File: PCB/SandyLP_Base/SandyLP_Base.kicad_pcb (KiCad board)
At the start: 2 copper layers, 275.5 x 80.3 mm, 228 parts, among them J1 Conn_01x10_Pin, J2 Conn_01x01_Pin, J3 Conn_02x02_Odd_Even, J7 USB_C_Receptacle_USB2.0, J8 Conn_01x03, Q1 BSS138, SW1 BOOT, SW3 BOOT_ALT, U1 NCP1117-3.3_SOT223, U2 RP2040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

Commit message: Mid-ISOの中央ネジがソケットのパッドに近すぎるので、少し上へ移動
USBのD+、D-なども合わせて調整。
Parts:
- moved H_mid_13 0.60 mm to (273.5, 45.5)
- moved H_mid_9 0.60 mm to (44.9, 45.5)
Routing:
- net D-: track 23.8 -> 24.4 mm
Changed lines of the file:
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@@
 		(fp_arc
 			(start -0.378178 -1.358526)
-			(mid -0.787709 -1.474533)
+			(mid -0.787708 -1.474533)
 			(end -0.8 -1.9)
 			(stroke
@@
 		(fp_arc
 			(start -0.378178 -1.358526)
-			(mid -0.787709 -1.474533)
+			(mid -0.787708 -1.474533)
 			(end -0.8 -1.9)
 			(stroke
@@
 	(footprint "locallib:MountingHole_1.8-2.2mm_M2_Pad_minimal"
 		(layer "B.Cu")
-		(at 44.870935 46.053405 180)
+		(at 44.870935 45.458102 180)
 		(descr "Mounting Hole 2.2mm, M2")
 		(tags "mounting hole 2.2mm m2")
@@
 	(footprint "locallib:MountingHole_1.8-2.2mm_M2_Pad_minimal"
 		(layer "B.Cu")
-		(at 273.470935 46.053405 180)
+		(at 273.470935 45.458102 180)
 		(descr "Mounting Hole 2.2mm, M2")
 		(tags "mounting hole 2.2mm m2")
@@
 	)
 	(segment
-		(start 51.428434 43.574655)
-		(end 42.524685 43.574655)
-		(width 0.5)
+		(start 35.045935 43.393813)
+		(end 35.045935 43.117115)
+		(width 0.381)
 		(layer "B.Cu")
 		(net 22)
 	)
 	(segment
-		(start 35.045935 43.393813)
-		(end 35.045935 43.117115)
-		(width 0.381)
+		(start 40.614685 45.484655)
+		(end 37.308435 45.484655)
+		(width 0.5)
 		(layer "B.Cu")
 		(net 22)
@@
 	)
 	(segment
-		(start 40.614685 45.484655)
-		(end 37.308435 45.484655)
-		(width 0.5)
+		(start 34.095935 42.092115)
+		(end 34.095935 43.121115)
+		(width 0.254)
 		(layer "B.Cu")
 		(net 22)
@@
 	)
 	(segment
-		(start 34.258435 43.184655)
-		(end 34.978395 43.184655)
-		(width 0.254)
+		(start 50.930629 43.07685)
+		(end 43.02249 43.07685)
+		(width 0.5)
+		(layer "B.Cu")
+		(net 22)
+	)
+	(segment
+		(start 43.02249 43.07685)
+		(end 40.614685 45.484655)
+		(width 0.5)
 		(layer "B.Cu")
 		(net 22)
@@
 	)
 	(segment
-		(start 34.095935 42.092115)
-		(end 34.095935 43.022155)
-		(width 0.254)
-		(layer "B.Cu")
-		(net 22)
-	)
-	(segment
-		(start 42.524685 43.574655)
-		(end 40.614685 45.484655)
+		(start 37.308435 45.484655)
+		(end 36.408435 46.384655)
 		(width 0.5)
 		(layer "B.Cu")
@@
 	)
 	(segment
-		(start 37.308435 45.484655)
-		(end 36.408435 46.384655)
-		(width 0.5)
+		(start 35.598935 43.946813)
+		(end 35.045935 43.393813)
+		(width 0.381)
 		(layer "B.Cu")
 		(net 22)
 	)
 	(segment
-		(start 34.095935 43.022155)
-		(end 34.258435 43.184655)
+		(start 35.095935 43.067115)
+		(end 35.045935 43.117115)
 		(width 0.254)
 		(layer "B.Cu")
@@
 	)
 	(segment
-		(start 35.598935 43.946813)
-		(end 35.045935 43.393813)
-		(width 0.381)
+		(start 35.095935 42.092115)
+		(end 35.095935 43.067115)
+		(width 0.254)
 		(layer "B.Cu")
 		(net 22)
 	)
 	(segment
-		(start 51.858435 44.004656)
-		(end 51.428434 43.574655)
-		(width 0.5)
+		(start 34.368633 43.393813)
+		(end 35.045935 43.393813)
+		(width 0.254)
 		(layer "B.Cu")
 		(net 22)
 	)
 	(segment
-		(start 35.095935 43.067115)
-		(end 35.045935 43.117115)
+		(start 34.095935 43.121115)
+		(end 34.368633 43.393813)
 		(width 0.254)
 		(layer "B.Cu")
@@
 	)
 	(segment
-		(start 35.095935 42.092115)
-		(end 35.095935 43.067115)
-		(width 0.254)
+		(start 51.858435 44.004656)
+		(end 50.930629 43.07685)
+		(width 0.5)
 		(layer "B.Cu")
 		(net 22)
@@
 	)
 	(segment
-		(start 49.370935 42.178405)
-		(end 49.870935 42.178405)
+		(start 44.858435 42.347155)
+		(end 45.258435 41.947155)
 		(width 0.5)
 		(layer "B.Cu")
@@
 	)
 	(segment
-		(start 36.808435 44.784655)
-		(end 40.324735 44.784655)
+		(start 40.324735 44.784655)
+		(end 43.162235 41.947155)
+		(width 0.5)
+		(layer "B.Cu")
+		(net 23)
+	)
+	(segment
+		(start 46.72874 42.37685)
+		(end 47.158435 41.947155)
+		(width 0.5)
+		(layer "B.Cu")
+		(net 23)
+	)
+	(segment
+		(start 43.162235 41.947155)
+		(end 43.858435 41.947155)
+		(width 0.5)
+		(layer "B.Cu")
+		(net 23)
+	)
+	(segment
+		(start 36.408435 44.384655)
+		(end 36.808435 44.784655)
+		(width 0.5)
+		(layer "B.Cu")
+		(net 23)
+	)
+	(segment
+		(start 43.858435 41.947155)
+		(end 44.258435 42.347155)
+		(width 0.5)
+		(layer "B.Cu")
+		(net 23)
+	)
+	(segment
+		(start 52.958435 42.647155)
+		(end 52.958435 44.004656)
+		(width 0.5)
+		(layer "B.Cu")
+		(net 23)
+	)
+	(segment
+		(start 45.82874 41.947155)
+		(end 46.258435 42.37685)
 		(width 0.5)
 		(layer "B.Cu")
@@
 	)
 	(segment
-		(start 51.670935 42.178405)
-		(end 52.620935 42.178405)
+		(start 48.658435 42.347155)
+		(end 49.058435 41.947155)
 		(width 0.5)
 		(layer "B.Cu")
@@
 	)
 	(segment
-		(start 34.595935 42.092115)
-		(end 34.595935 41.247155)
-		(width 0.254)
+		(start 48.158435 42.347155)
+		(end 48.658435 42.347155)
+		(width 0.5)
 		(layer "B.Cu")
 		(net 23)
 	)
 	(segment
-		(start 51.220935 42.628405)
-		(end 51.670935 42.178405)
-		(width 0.5)
+		(start 34.595935 42.092115)
+		(end 34.595935 41.247155)
+		(width 0.254)
 		(layer "B.Cu")
 		(net 23)
 	)
 	(segment
-		(start 53.290935 43.672156)
-		(end 52.958435 44.004656)
+		(start 47.158435 41.947155)
+		(end 47.758435 41.947155)
 		(width 0.5)
 		(layer "B.Cu")
@@
 	)
 	(segment
-		(start 50.320935 42.628405)
-		(end 51.220935 42.628405)
+		(start 50.358435 42.347155)
+		(end 52.658435 42.347155)
 		(width 0.5)
 		(layer "B.Cu")
@@
 	)
 	(segment
-		(start 53.290935 42.848405)
-		(end 53.290935 43.672156)
+		(start 46.258435 42.37685)
+		(end 46.72874 42.37685)
 		(width 0.5)
 		(layer "B.Cu")
@@
 	)
 	(segment
-		(start 42.234735 42.874655)
-		(end 48.674685 42.874655)
+		(start 52.658435 42.347155)
+		(end 52.958435 42.647155)
+		(width 0.5)
+		(layer "B.Cu")
+		(net 23)
+	)
+	(segment
+		(start 36.808435 44.784655)
+		(end 40.324735 44.784655)
 		(width 0.5)
 		(layer "B.Cu")
@@
 	)
 	(segment
-		(start 52.620935 42.178405)
-		(end 53.290935 42.848405)
+		(start 44.258435 42.347155)
+		(end 44.858435 42.347155)
 		(width 0.5)
 		(layer "B.Cu")
@@
 	)
 	(segment
-		(start 49.870935 42.178405)
-		(end 50.320935 42.628405)
+		(start 49.058435 41.947155)
+		(end 49.958435 41.947155)
 		(width 0.5)
 		(layer "B.Cu")
@@
 	)
 	(segment
-		(start 40.324735 44.784655)
-		(end 42.234735 42.874655)
+		(start 49.958435 41.947155)
+		(end 50.358435 42.347155)
 		(width 0.5)
 		(layer "B.Cu")
@@
 	)
 	(segment
-		(start 36.408435 44.384655)
-		(end 36.808435 44.784655)
+		(start 47.758435 41.947155)
+		(end 48.158435 42.347155)
 		(width 0.5)
 		(layer "B.Cu")
@@
 	)
 	(segment
-		(start 48.674685 42.874655)
-		(end 49.370935 42.178405)
+		(start 45.258435 41.947155)
+		(end 45.82874 41.947155)
 		(width 0.5)
 		(layer "B.Cu")
@@
 	)
 	(via
-		(at 41.970935 42.028405)
+		(at 41.89439 41.886224)
 		(size 0.8)
 		(drill 0.4)
@@
 	)
 	(via
+		(at 53.508435 41.697155)
+		(size 0.8)
+		(drill 0.4)
+		(layers "F.Cu" "B.Cu")
+		(free yes)
+		(net 91)
+	)
+	(via
 		(at 23.870935 44.928405)
 		(size 0.8)
@@
 	)
 	(via
-		(at 52.270935 43.118405)
-		(size 0.8)
-		(drill 0.4)
-		(layers "F.Cu" "B.Cu")
-		(free yes)
-		(net 91)
-	)
-	(via
 		(at 159.171051 113.919101)
 		(size 0.8)
@@
 	)
 	(via
-		(at 37.608435 43.934655)
+		(at 37.458435 43.934655)
 		(size 0.8)
 		(drill 0.4)
@@
 	)
 	(via
-		(at 50.770935 41.628405)
+		(at 48.408435 41.147155)
 		(size 0.8)
 		(drill 0.4)
@@
 	)
 	(via
-		(at 44.870935 41.978405)
+		(at 44.558435 41.147155)
 		(size 0.8)
 		(drill 0.4)
@@
 	)
 	(via
-		(at 48.270935 41.978405)
+		(at 46.508435 41.147155)
 		(size 0.8)
 		(drill 0.4)
@@
 	)
 	(via
-		(at 53.370935 41.628405)
+		(at 51.158435 41.147155)
 		(size 0.8)
 		(drill 0.4)
@@
 	)
 	(via
-		(at 54.270935 43.128405)
+		(at 54.058435 43.128405)
 		(size 0.8)
 		(drill 0.4)

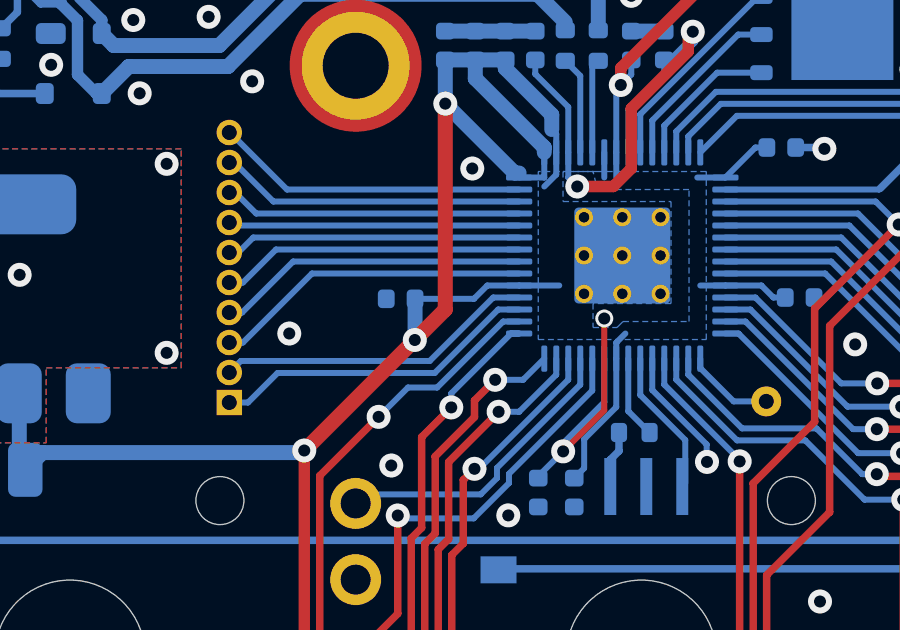
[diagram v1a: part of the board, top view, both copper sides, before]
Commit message: MCUまわりのCを近づける
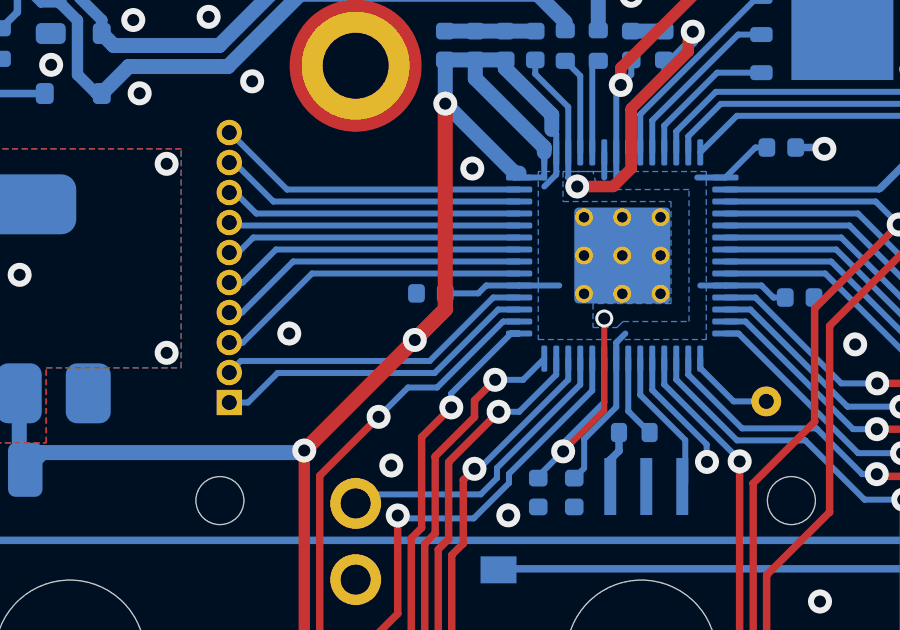
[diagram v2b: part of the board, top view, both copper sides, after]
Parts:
- moved C8 1.02 mm to (47.4, 53.0)
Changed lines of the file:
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@@
 		(fp_arc
 			(start -0.378178 -1.358526)
-			(mid -0.787708 -1.474533)
+			(mid -0.787709 -1.474533)
 			(end -0.8 -1.9)
 			(stroke
@@
 		(fp_arc
 			(start -0.378178 -1.358526)
-			(mid -0.787708 -1.474533)
+			(mid -0.787709 -1.474533)
 			(end -0.8 -1.9)
 			(stroke
@@
 	(footprint "Capacitor_SMD:C_0402_1005Metric"
 		(layer "B.Cu")
-		(at 46.370935 53.228405 180)
+		(at 47.378435 53.047155 180)
 		(descr "Capacitor SMD 0402 (1005 Metric), square (rectangular) end terminal, IPC_7351 nominal, (Body size source: IPC-SM-782 page 76, https://www.pcb-3d.com/wordpress/wp-content/uploads/ipc-sm-782a_amendment_1_and_2.pdf), generated with kicad-footprint-generator")
 		(tags "capacitor")
@@
 	)
 	(segment
-		(start 48.814685 53.228405)
-		(end 46.850935 53.228405)
-		(width 0.2)
-		(layer "B.Cu")
-		(net 1)
-	)
-	(segment
 		(start 57.195935 49.184655)
 		(end 58.195935 48.184655)
@@
 	)
 	(segment
+		(start 46.842809 54.600281)
+		(end 47.858435 53.584655)
+		(width 0.5)
+		(layer "B.Cu")
+		(net 1)
+	)
+	(segment
 		(start 55.878435 41.364655)
 		(end 55.858435 41.344655)
@@
 	)
 	(segment
-		(start 46.850935 54.592155)
-		(end 46.842809 54.600281)
+		(start 47.858435 45.264655)
+		(end 49.858435 45.264655)
 		(width 0.5)
 		(layer "B.Cu")
@@
 	)
 	(segment
-		(start 47.858435 45.264655)
-		(end 49.858435 45.264655)
-		(width 0.5)
+		(start 50.320935 52.784655)
+		(end 49.220935 52.784655)
+		(width 0.2)
 		(layer "B.Cu")
 		(net 1)
@@
 	)
 	(segment
-		(start 46.850935 53.228405)
-		(end 46.850935 54.592155)
-		(width 0.5)
-		(layer "B.Cu")
-		(net 1)
-	)
-	(segment
 		(start 58.195935 48.184655)
 		(end 58.578435 48.184655)
@@
 	)
 	(segment
-		(start 49.258435 52.784655)
-		(end 48.814685 53.228405)
-		(width 0.2)
-		(layer "B.Cu")
-		(net 1)
-	)
-	(segment
 		(start 53.558435 55.222155)
 		(end 53.558435 54.688295)
@@
 	)
 	(segment
+		(start 49.220935 52.784655)
+		(end 48.958435 53.047155)
+		(width 0.2)
+		(layer "B.Cu")
+		(net 1)
+	)
+	(segment
 		(start 51.408435 47.094654)
 		(end 51.408435 47.584655)
@@
 	)
 	(segment
-		(start 50.320935 52.784655)
-		(end 49.258435 52.784655)
-		(width 0.2)
+		(start 47.858435 53.584655)
+		(end 47.858435 53.047155)
+		(width 0.5)
 		(layer "B.Cu")
 		(net 1)
@@
 		(width 0.2)
 		(layer "B.Cu")
+		(net 1)
+	)
+	(segment
+		(start 48.958435 53.047155)
+		(end 47.858435 53.047155)
+		(width 0.2)
+		(layer "B.Cu")

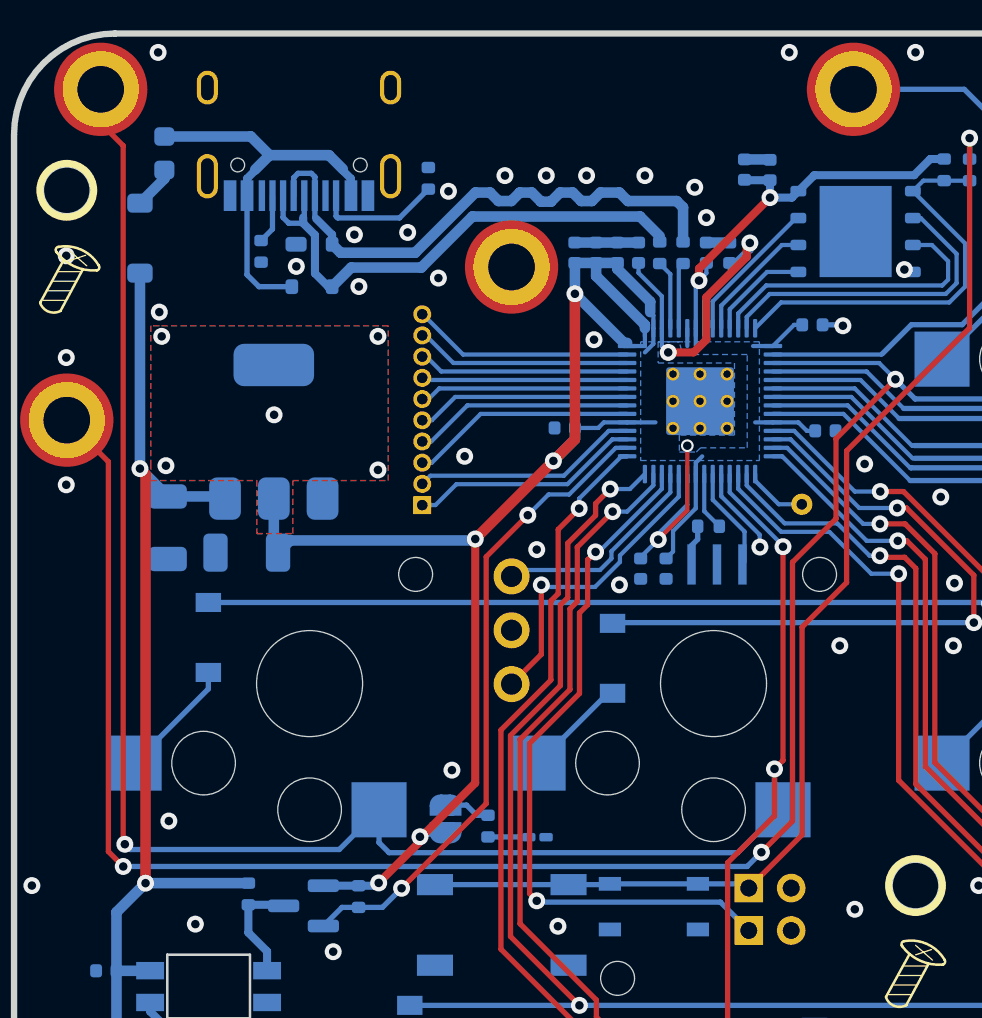
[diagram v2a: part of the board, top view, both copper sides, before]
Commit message: USB配線まわりを、ネジ穴、ナット、使用する工具（十字レンチなど）から離す
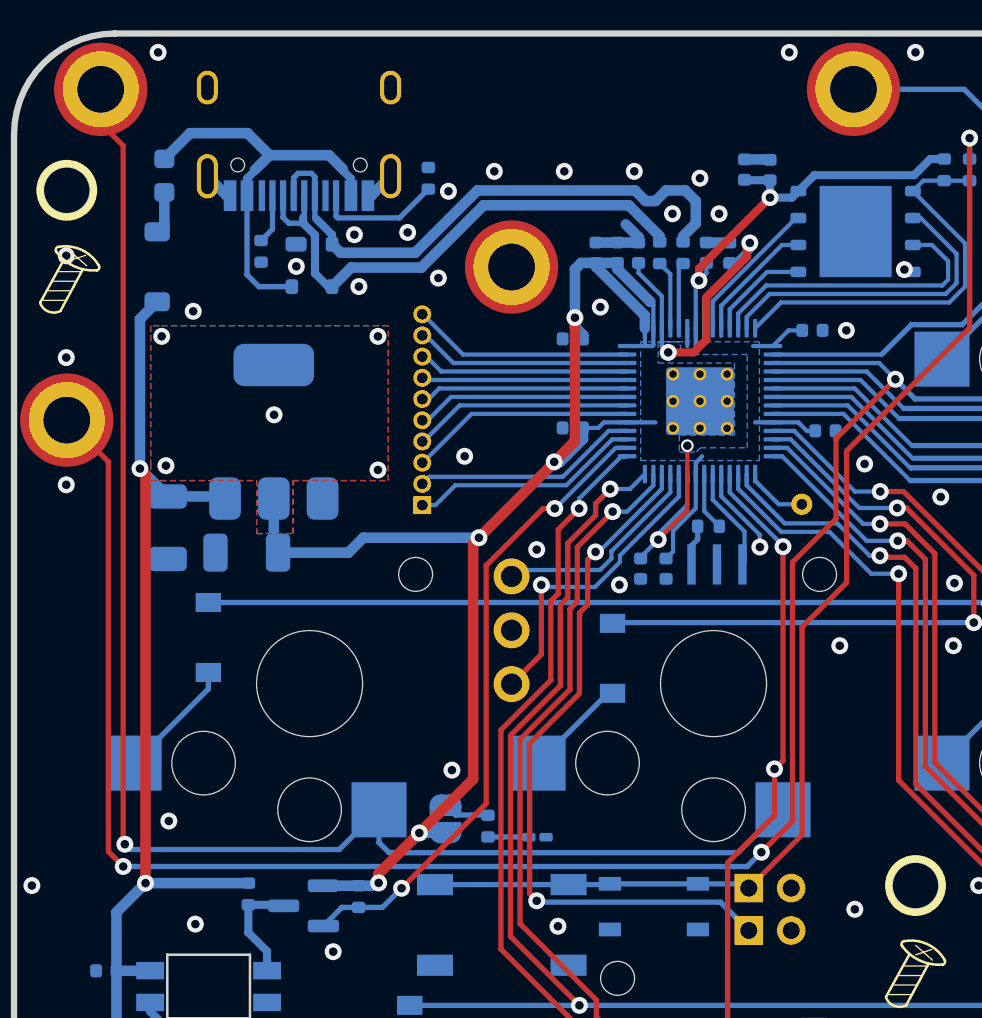
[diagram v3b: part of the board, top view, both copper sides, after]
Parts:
- moved C7 4.06 mm to (47.8, 48.8), turned to 180 degrees
- moved SD1 1.58 mm to (28.2, 45.4)
- moved F1 1.06 mm to (28.5, 41.1)
- moved REF** 0.68 mm to (44.9, 48.9)
- moved REF** 0.64 mm to (45.3, 50.5)
- moved REF** 0.42 mm to (27.3, 52.6)
- moved REF** 0.42 mm to (27.8, 54.2)
- moved C8 0.38 mm to (47.8, 53.0)
- moved REF** 0.29 mm to (28.6, 35.9)
- moved C11 0.26 mm to (59.1, 48.4)
- moved REF** 0.20 mm to (28.9, 38.2)
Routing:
- net +3V3: track 103.9 -> 101.3 mm
- net GND: track 10.5 -> 12.5 mm
- net +5V: track 334.4 -> 333.4 mm
- net VBUS: track 18.9 -> 19.5 mm
- net D+: track 26.1 -> 26.6 mm

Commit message: LEDのパスコンを基板端から離して調整
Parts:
- moved C14 1.84 mm to (27.0, 77.2)
- moved C15 1.84 mm to (27.0, 82.0)
- moved C18 1.78 mm to (27.0, 86.8)
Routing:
- net +5V: track 333.4 -> 331.0 mm
- net GND: vias 145 -> 144
